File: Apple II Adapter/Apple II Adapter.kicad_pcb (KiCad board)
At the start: 2 copper layers, 59.7 x 41.3 mm, 23 parts, among them J1 IDC_PORT1, J2 IDC_PORT2, M1 Mounting, U1 74HCT04, U2 CD4066

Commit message: Added license label
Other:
- board text added: "Licensed under CERN OHL v1.2"

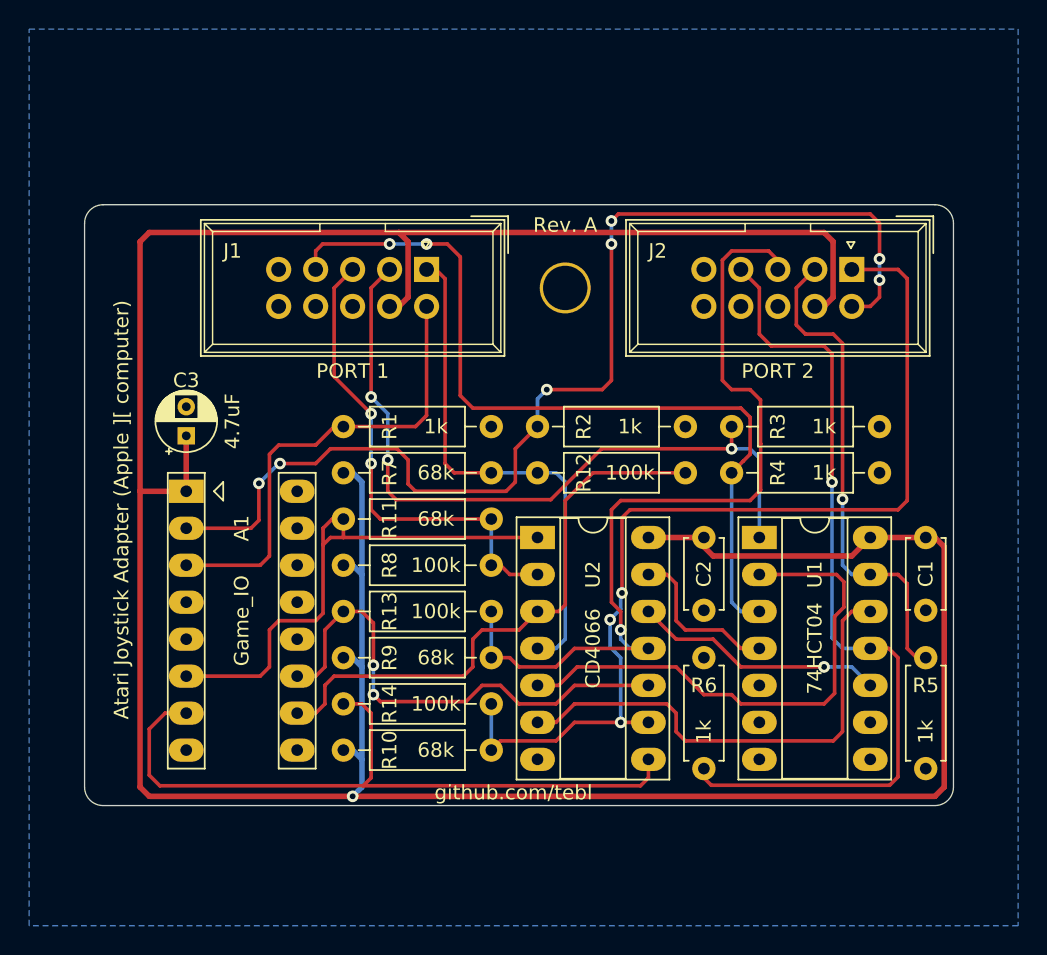
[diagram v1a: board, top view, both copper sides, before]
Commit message: Fixed revision A bugs (label and joystick common)
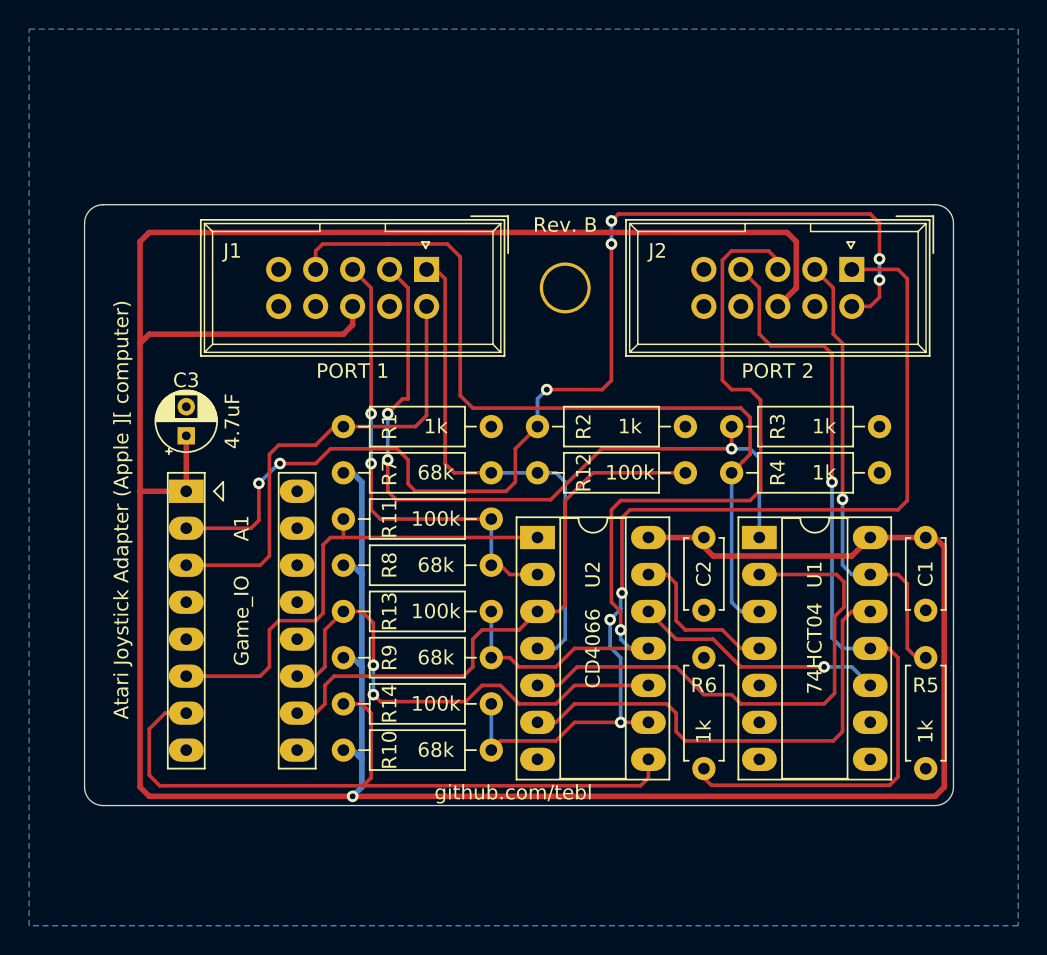
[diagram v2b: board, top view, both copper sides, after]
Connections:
- J1 pad 7: VCC -> (no net)
- J1 pad 8: GND -> VCC
- J2 pad 7: VCC -> (no net)
- J2 pad 8: GND -> VCC
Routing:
- net VCC: track 226.4 -> 233.7 mm
- net /GC0: track 36.4 -> 33.6 mm
- net /P2_DOWN: track 34.2 -> 32.1 mm
- net /P1_LEFT: track 33.2 -> 32.2 mm
- net /P1_RIGHT: track 57.2 -> 57.5 mm, vias 2 -> 0
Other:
- board text added: "Rev. B"
- board text removed: "Rev. A"

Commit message: Swapped fire buttons
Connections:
- A1 pad 2: /P2_FIRE -> /P1_FIRE
- A1 pad 3: /P1_FIRE -> /P2_FIRE
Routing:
- net /P2_FIRE: track 78.5 -> 82.1 mm, vias 7 -> 5
- net /P1_FIRE: track 32.4 -> 30.6 mm
